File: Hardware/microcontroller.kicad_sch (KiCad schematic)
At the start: 66 parts, among them J1 FTSH-105-X-X-DV-007-P-X, SW1 208-4, U1 STM32F407VGT6, U2 SIT1566AC-JV-XXE-32.768D

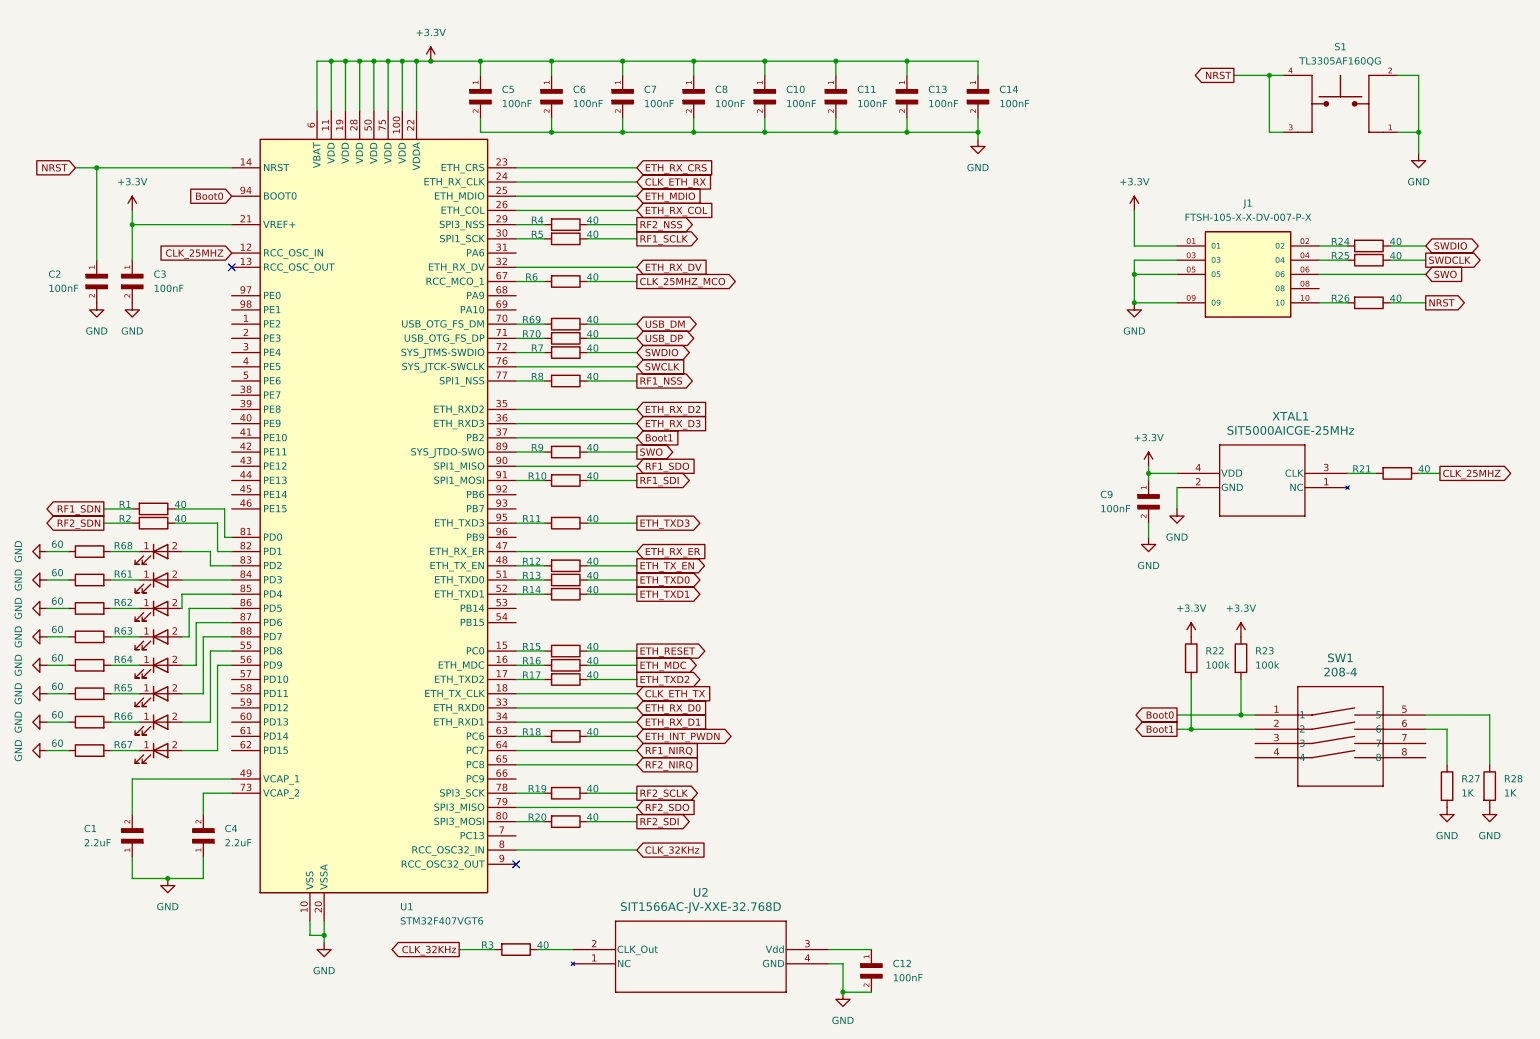
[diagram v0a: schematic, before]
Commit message: added stackup doc and reduced board to 10 layers
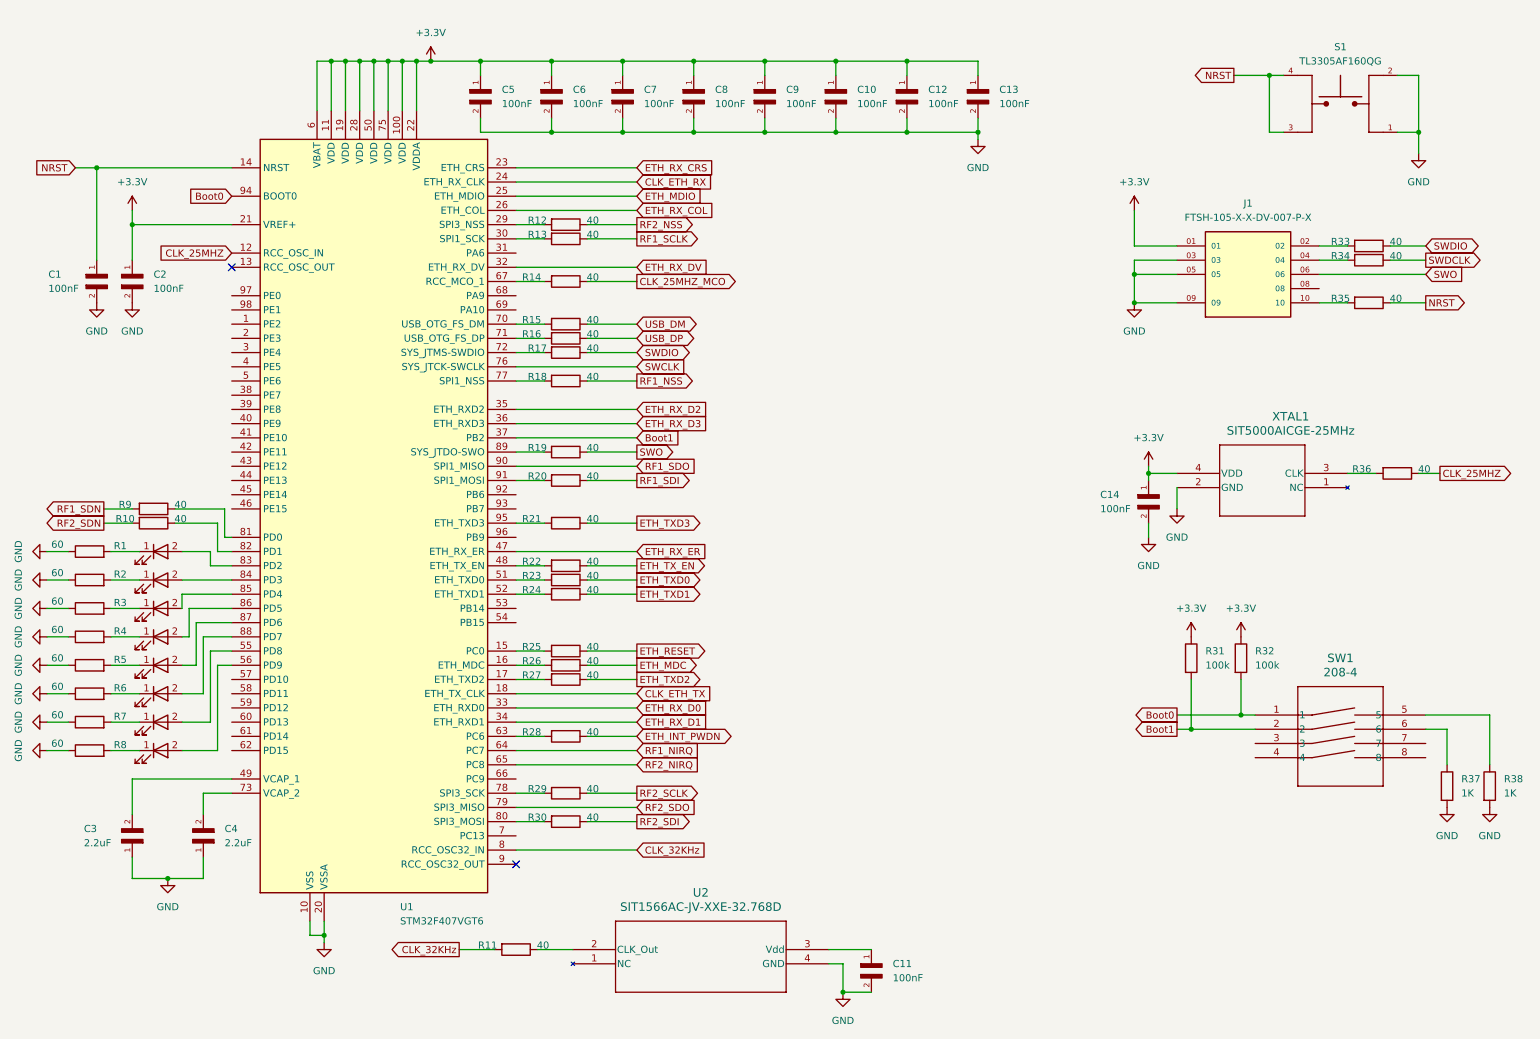
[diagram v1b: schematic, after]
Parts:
- renumbered C2 to C1, C11 to C10, C12 to C11, C13 to C12, C14 to C13, C9 to C14, C3 to C2, C1 to C3, C10 to C9, LED9 to LED1, R68 to R1, R2 to R10, R3 to R11, R4 to R12, R5 to R13, R6 to R14, R69 to R15, R70 to R16, R7 to R17, R8 to R18, R9 to R19, R61 to R2, R10 to R20, R11 to R21, R12 to R22, R13 to R23, R14 to R24, R15 to R25, R16 to R26, R17 to R27, R18 to R28, R19 to R29, R62 to R3, R20 to R30, R22 to R31, R23 to R32, R24 to R33, R25 to R34, R26 to R35, R21 to R36, R27 to R37, R28 to R38, R63 to R4, R64 to R5, R65 to R6, R66 to R7, R67 to R8, R1 to R9

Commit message: initial 8 layer layout with power decoupling connections
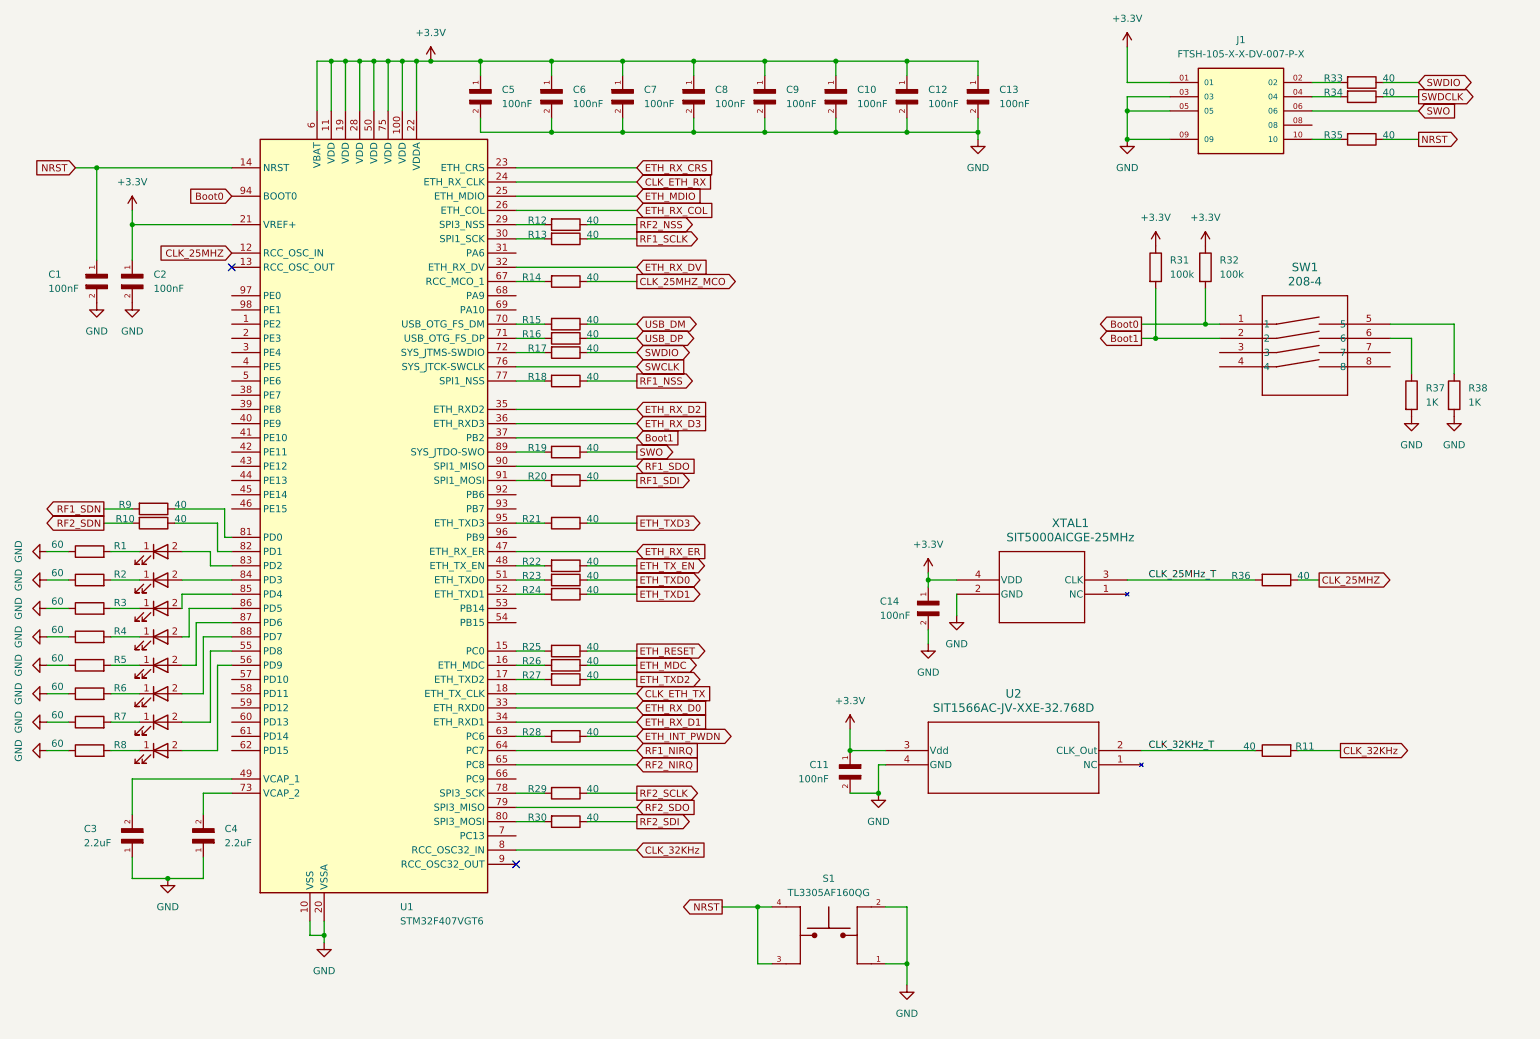
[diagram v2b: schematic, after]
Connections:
- net +3.3V: now also C11.1, U2.3 (Vdd)
- net CLK_32KHz_T: now reaches R11.1, U2.2 (CLK_Out)
- net CLK_25MHz_T: now reaches R36.2, XTAL1.3 (CLK)
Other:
- moved on the sheet: C11, C14, J1, R11, R31, R32, R33, R34, R35, R36, R37, R38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

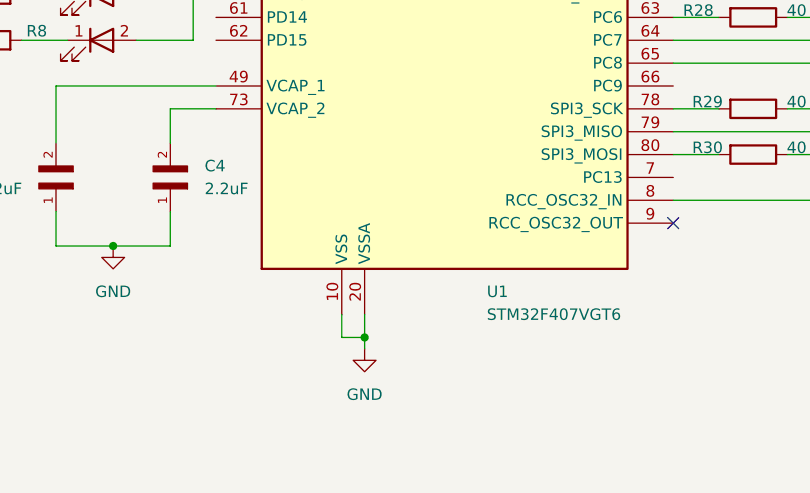
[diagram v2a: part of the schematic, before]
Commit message: fixed USB data lines and directory hierarchy
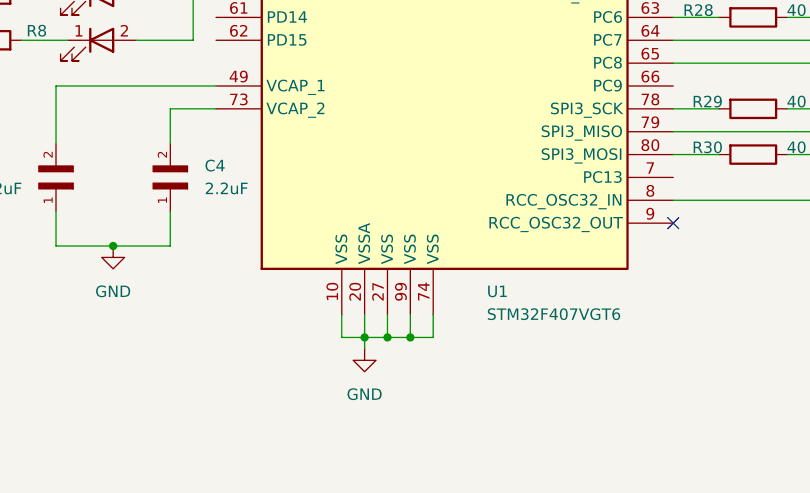
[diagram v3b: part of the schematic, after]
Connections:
- net GND: now also U1.27 (VSS), U1.74 (VSS), U1.99 (VSS)
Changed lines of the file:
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@@
+	)
+	(junction
+		(at 73.66 180.34)
+		(diameter 0)
+		(color 0 0 0 0)
 	)
 	(junction
@@
 	(junction
 		(at 74.93 24.13)
+		(diameter 0)
+		(color 0 0 0 0)
+	)
+	(junction
+		(at 71.12 180.34)
 		(diameter 0)
 		(color 0 0 0 0)
@@
 	(wire
 		(pts
+			(xy 73.66 180.34) (xy 76.2 180.34)
+		)
+		(stroke
+			(width 0)
+			(type default)
+		)
+	)
+	(wire
+		(pts
 			(xy 68.58 180.34) (xy 68.58 181.61)
 		)
@@
 	(wire
 		(pts
+			(xy 68.58 180.34) (xy 71.12 180.34)
+		)
+		(stroke
+			(width 0)
+			(type default)
+		)
+	)
+	(wire
+		(pts
 			(xy 22.86 147.32) (xy 19.05 147.32)
 		)
@@
 	(wire
 		(pts
+			(xy 73.66 180.34) (xy 73.66 177.8)
+		)
+		(stroke
+			(width 0)
+			(type default)
+		)
+	)
+	(wire
+		(pts
 			(xy 85.09 24.13) (xy 87.63 24.13)
 		)
@@
 	(wire
 		(pts
+			(xy 71.12 180.34) (xy 71.12 177.8)
+		)
+		(stroke
+			(width 0)
+			(type default)
+		)
+	)
+	(wire
+		(pts
 			(xy 212.09 38.1) (xy 219.71 38.1)
 		)
@@
 	(wire
 		(pts
+			(xy 76.2 180.34) (xy 76.2 177.8)
+		)
+		(stroke
+			(width 0)
+			(type default)
+		)
+	)
+	(wire
+		(pts
 			(xy 22.86 137.16) (xy 19.05 137.16)
 		)
@@
 		)
 		(stroke
+			(width 0)
+			(type default)
+		)
+	)
+	(wire
+		(pts
+			(xy 71.12 180.34) (xy 73.66 180.34)
+		)
+		(stroke
